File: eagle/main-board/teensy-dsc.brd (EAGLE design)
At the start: 85 x 55 mm, 29 parts, among them J1 RJ11-6PTH, J2 RJ11-6PTH, J3 RJ45-8PTH, J4 POWER_JACKPTH, J5 USB-B, Q1 IRLML6344, X1 STEREOJACK, X2 STEREOJACK

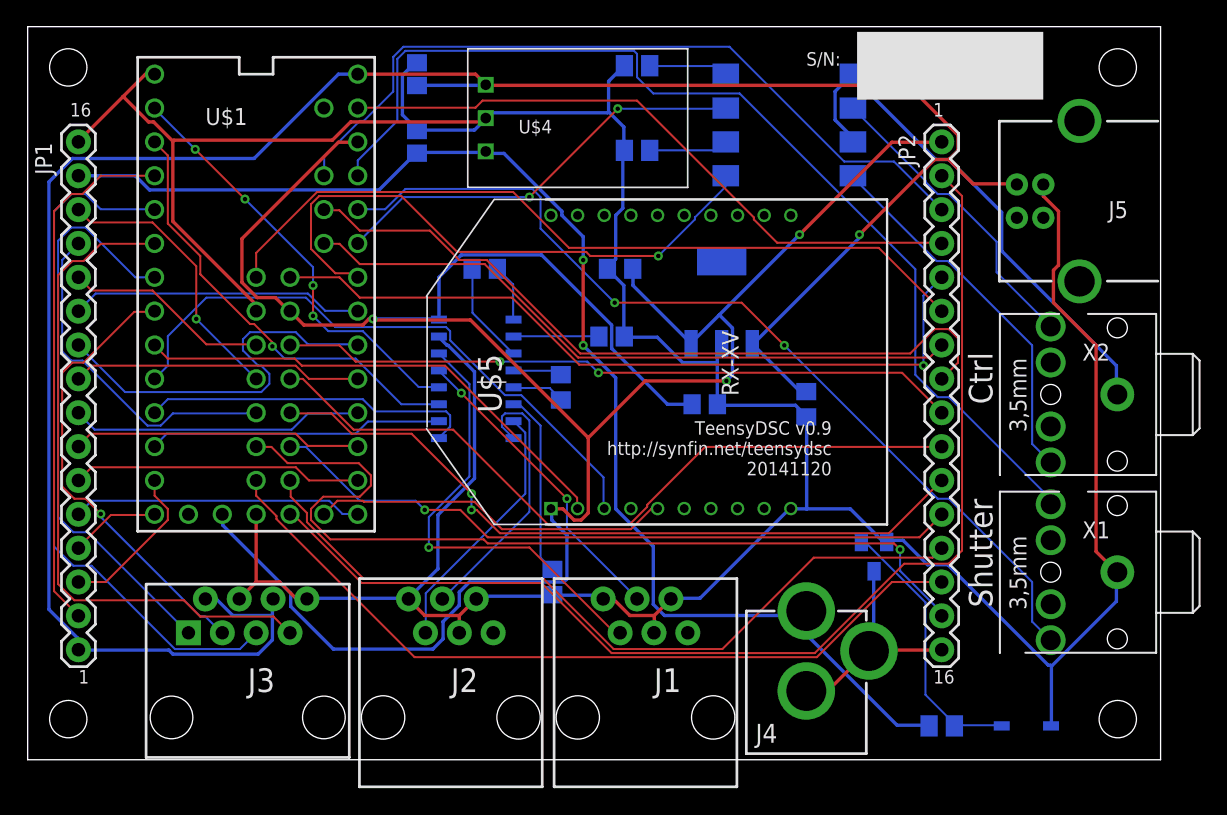
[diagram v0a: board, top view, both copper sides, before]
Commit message: Initial WizFi210/220 redesign
Also fixes naming of various Teensy pins which were wrong
or incorrectly routed for serial ports/shutter/focus per
the Google doc.
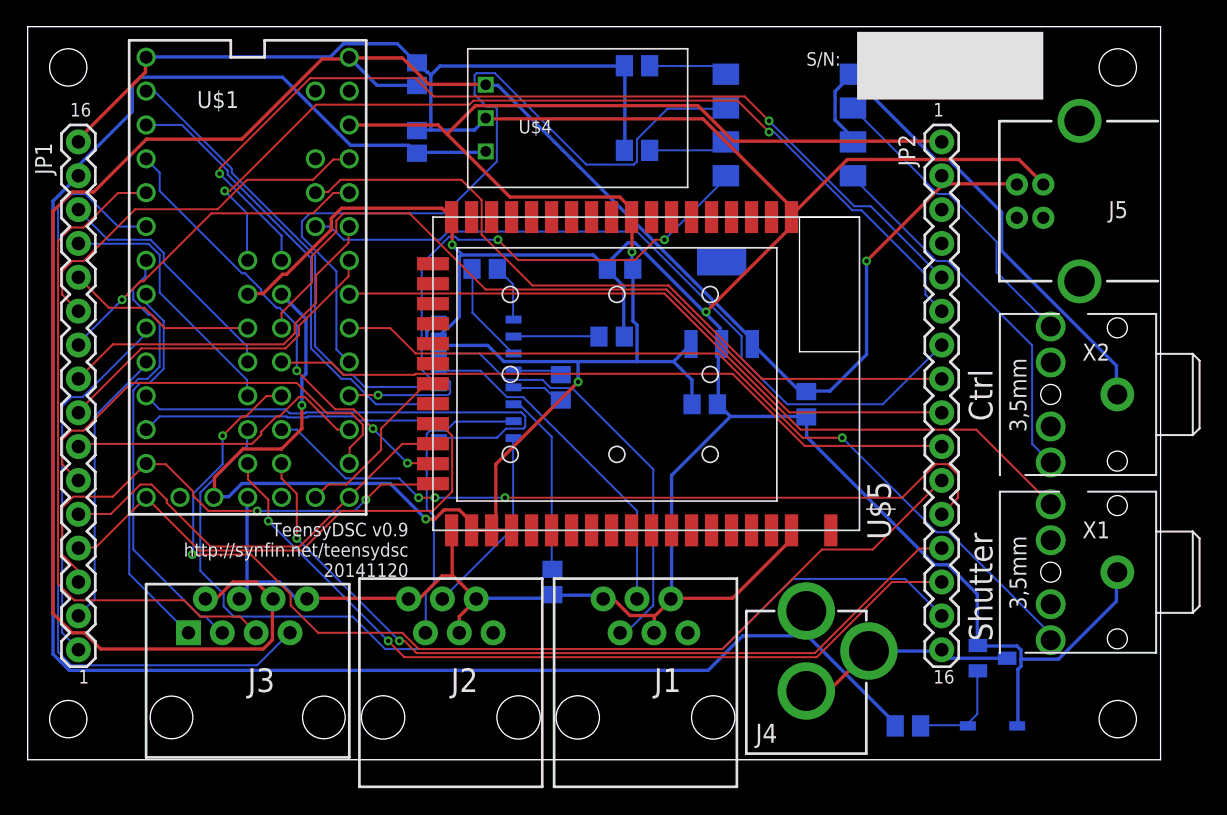
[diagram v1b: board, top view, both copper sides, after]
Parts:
- U$5: value XBEERX-VN -> (none); device xbee_r1:RX-VN -> WizFi210:WIZFI210/220
- moved U$5 22.4 mm to (29.2, 41.9), turned to 270 degrees
- moved Q1 11.7 mm to (72.4, 7.62), turned to 90 degrees
- moved D5 2.54 mm to (72.4, 2.54)
- moved R15 2.54 mm to (66.0, 2.54)
- moved U$1 1.42 mm to (16.5, 34.9)
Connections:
- net P14 renamed LCD_DC
- net P15 renamed LCD_CS
- net P24 renamed TEMP
- net P25 renamed C1
- net P26 renamed C2
- net P27 renamed D1
- net P28 renamed D2
- net P29 renamed C_BUTTON
- net P30 renamed D_BUTTON
- net P31 renamed BATTMON
- net P33 renamed LCD_RESET
- removed net FOCUS-CTL: U$1.20/A6, U$6.1
- removed net P11: JP1.14, U$1.11
- removed net P12: JP1.13, U$1.12
- removed net P13: JP1.12, U$1.13
- removed net P16: JP1.9, U$1.16/A2
- removed net P17: JP1.8, U$1.17/A3
- removed net P18: JP1.7, U$1.18/A4
- removed net P19: JP1.6, U$1.19/A5
- removed net P2: JP1.15, U$1.2
- removed net PGM: JP2.2, U$1.PGM
- removed net SHUTTER-CTL: U$1.21/A7, U$6.3
- removed net XBEE_IN: U$1.8, U$5.3
- removed net XBEE_OUT: U$1.7, U$5.2
- removed net XBEE_RST: U$1.A14, U$5.5
- new net DEW1: JP1.9, U$1.20/A6
- new net DEW2: JP1.8, U$1.21/A7
- new net DEW3: JP1.7, U$1.22/A8
- new net DEW4: JP1.6, U$1.23/A9
- new net FOCUS_CTL: U$1.16/A2, U$6.1
- new net MISO: JP1.13, U$1.12, U$5.27
- new net MOSI: JP1.14, U$1.11, U$5.30
- new net RX3: JP1.16, U$1.7
- new net SCK: JP1.12, U$1.13, U$5.28
- new net SHUTTER_CTL: U$1.17/A3, U$6.3
- new net TX3: JP1.15, U$1.8
- new net WIZNET_CS: U$1.2, U$5.29
- new net WIZNET_FACRESET: U$1.A14, U$5.25
- net 3.3V: now also U$5.32, U$5.33, U$5.34, U$5.9; no longer U$5.1
- net 5V: now also JP2.2; no longer JP1.16
- net AGND: no longer JP2.4
- net AREF: no longer JP2.3
- net GND: now also U$5.1, U$5.18, U$5.31, U$5.48; no longer U$5.10
- net SW1: now also U$1.18/A4; no longer U$1.22/A8
- net SW2: now also U$1.19/A5; no longer U$1.23/A9
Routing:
- net PGM: track 86.7 -> 0.00 mm
- net SHUTTER_CTL: track 0.00 -> 60.5 mm
- net AREF: track 57.8 -> 0.00 mm
- net AGND: track 48.6 -> 0.00 mm
- net +12V: track 98.1 -> 145.6 mm, vias 2 -> 0
- net FOCUS_CTL: track 0.00 -> 46.1 mm, vias 0 -> 3
- net XBEE_IN: track 45.9 -> 0.00 mm
- net FOCUS-CTL: track 44.1 -> 0.00 mm, vias 1 -> 0
- net GND: track 270.6 -> 312.6 mm, vias 0 -> 2
- net P2: track 39.8 -> 0.00 mm
- net MISO: track 0.00 -> 39.1 mm
- net MOSI: track 0.00 -> 37.8 mm, vias 0 -> 2
- net XBEE_OUT: track 37.3 -> 0.00 mm
- net WIZNET_CS: track 0.00 -> 34.0 mm, vias 0 -> 3
- net SCK: track 0.00 -> 32.8 mm
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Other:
- board text added: "Serial"
- board text added: "Serial1"
- board text added: "Serial2"

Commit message: more WizFi updates....
After further research, I'm not convinced the WizFi is the way to go.
Most likely will need to replace it with something else if I want
to support serial ports.  Probably should move the serial ports
to a daughter board.
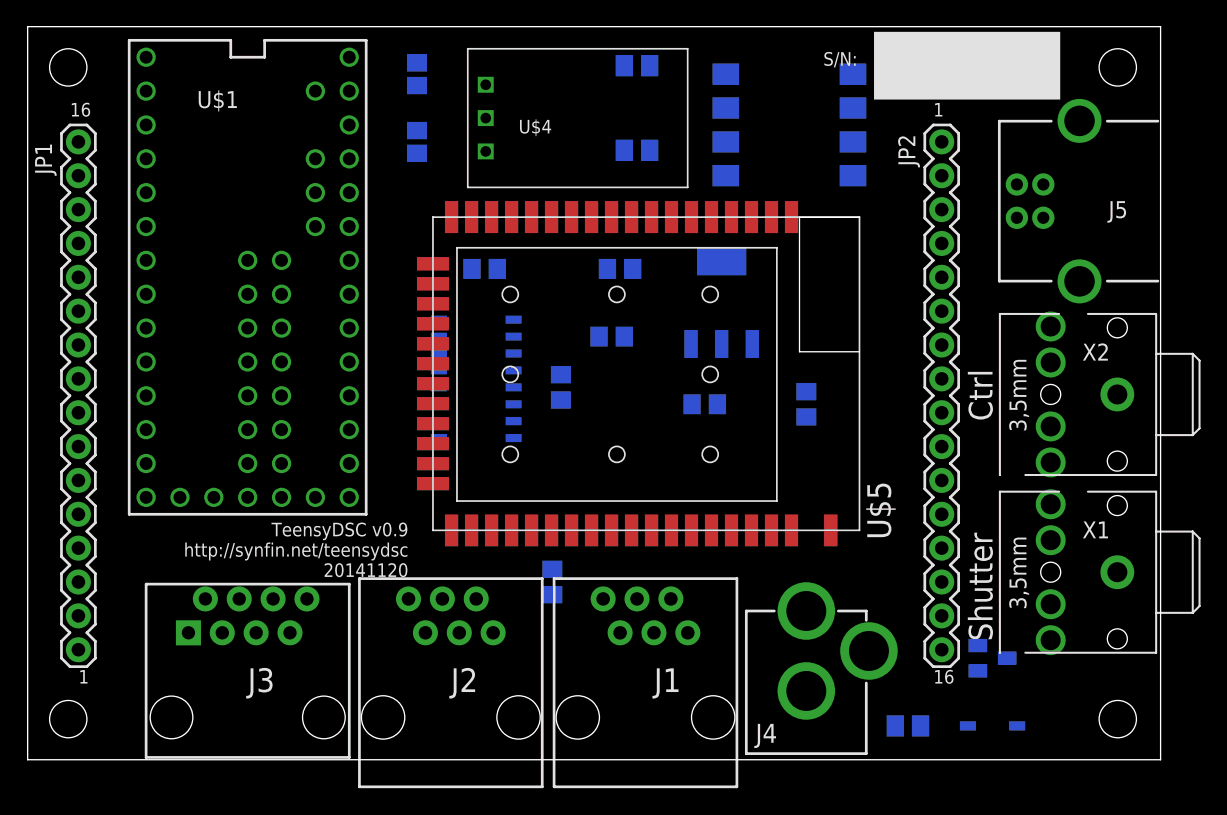
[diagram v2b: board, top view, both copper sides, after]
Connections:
- net C1 renamed ENC_C1
- net C2 renamed ENC_C2
- net C_BUTTON renamed D29/A18
- net D1 renamed ENTER
- net D2 renamed BACK
- net D_BUTTON renamed D30/A19
- net P32 renamed D32
- new net WIZFI_DR: U$5.23
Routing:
- net GND: track 312.6 -> 0.00 mm, vias 2 -> 0
- net 5V: track 162.8 -> 0.00 mm, vias 1 -> 0
- net 3.3V: track 162.6 -> 0.00 mm, vias 4 -> 0
- net +12V: track 145.6 -> 0.00 mm
- net BATTMON: track 80.4 -> 0.00 mm, vias 2 -> 0
- net ENTER: track 74.0 -> 0.00 mm
- net A13: track 72.0 -> 0.00 mm, vias 2 -> 0
- net A12: track 70.0 -> 0.00 mm, vias 2 -> 0
- net SW1: track 62.6 -> 0.00 mm, vias 1 -> 0
- net BACK: track 62.0 -> 0.00 mm, vias 2 -> 0
- net LCD_RESET: track 61.6 -> 0.00 mm
- net D29/A18: track 61.3 -> 0.00 mm, vias 2 -> 0
- net SHUTTER_CTL: track 60.5 -> 0.00 mm
- net CHAN-A-ALT/DEC: track 60.2 -> 0.00 mm
- net SW2: track 59.2 -> 0.00 mm
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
